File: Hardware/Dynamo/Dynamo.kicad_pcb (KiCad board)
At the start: 2 copper layers, 69.2 x 53.9 mm, 50 parts, among them U1 AP63205WU, U10 ESP32-S3-WROOM-1, U11 NCP1117-3.3_SOT223, U12 74AHC1G32, U13 TXS0102DCT, U14 TXS0102DCT, U15 74AHC1G32, U16 74AHC1G32, U17 74AHC1G32, U2 TLP2770, U3 TLP2770, U4 74LVC1G86, U5 74LVC1G86, U6 74LVC1G86, U7 74LVC1G86, U8 74LVC1G86, U9 74LVC1G86

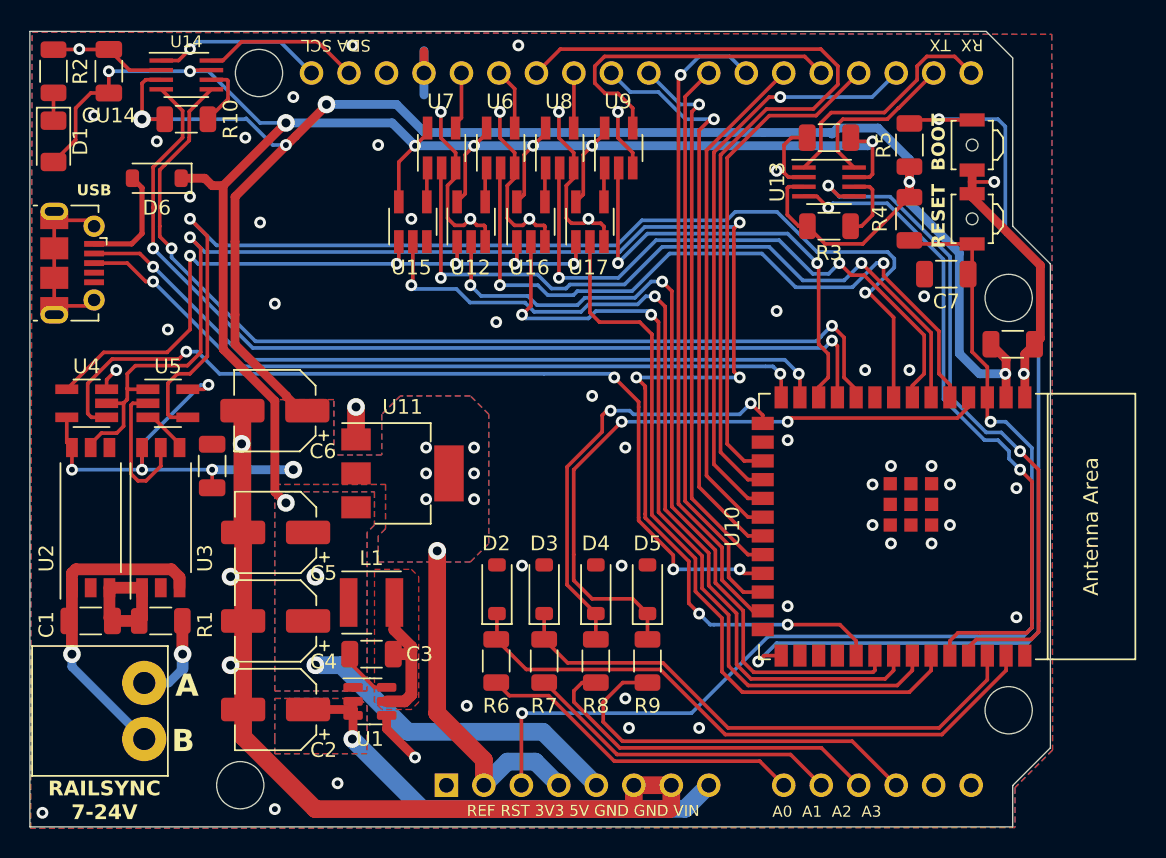
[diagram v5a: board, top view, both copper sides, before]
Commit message: Change Railsync input to use same 3.5mm connector as EX8874 outputs
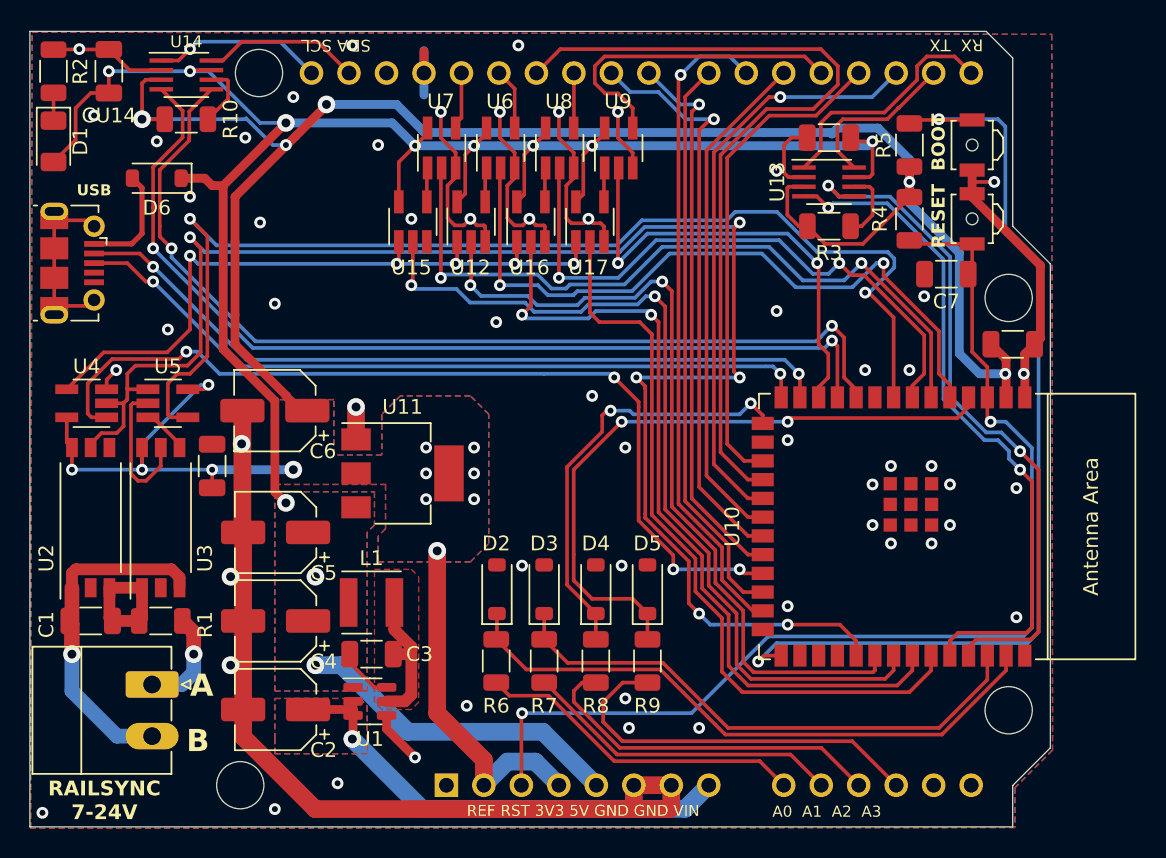
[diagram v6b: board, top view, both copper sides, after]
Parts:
- Railsync1: value WR-TBL 2P -> 2P 5mm; footprint Terminal_Wuerth_new:WR-TBL 2P -> Connector_Phoenix_MC:PhoenixContact_MC_1,5_2-G-3.5_1x02_P3.50mm_Horizontal
- moved Railsync1 3.96 mm to (129.9, 93.1)
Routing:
- net /RAILSYNC_B: track 21.6 -> 25.3 mm
- net /RAILSYNC_A: track 6.25 -> 6.97 mm

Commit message: Revised 5v regulator, layout refinement.
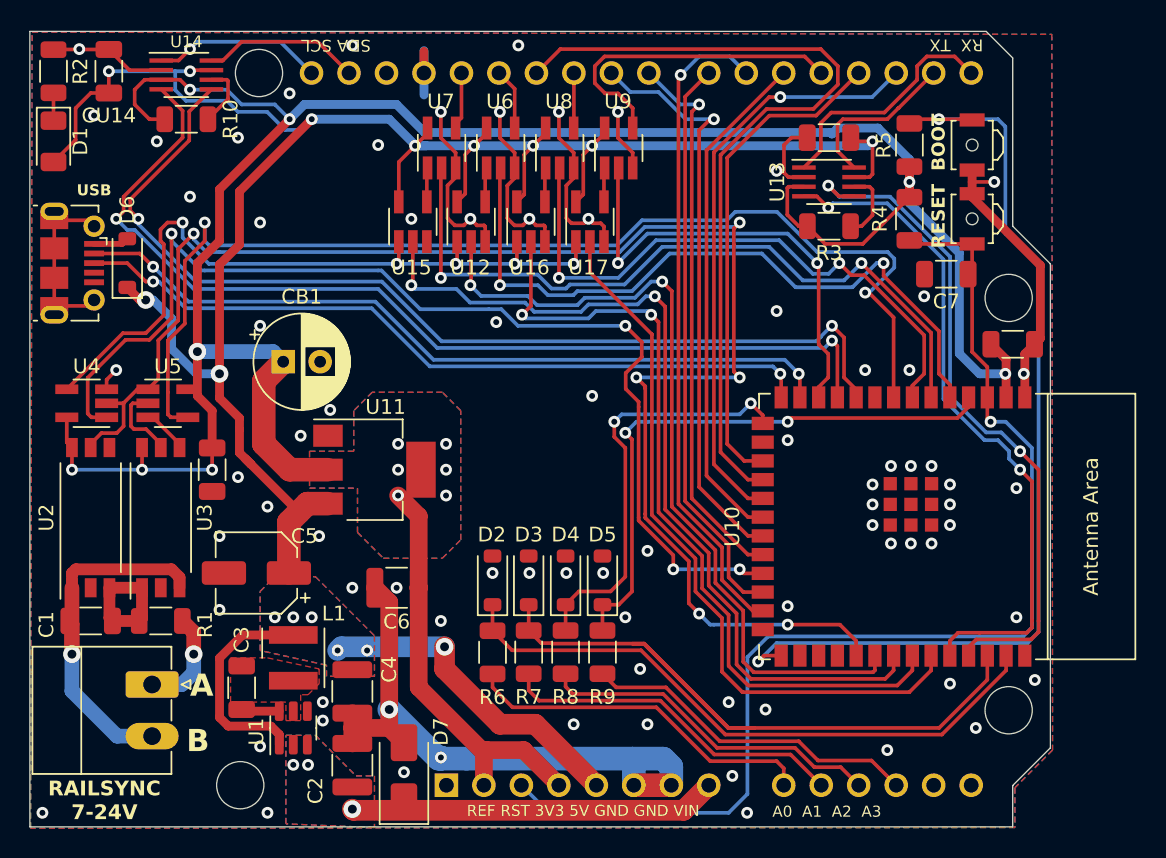
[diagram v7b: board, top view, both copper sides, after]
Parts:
- added CB1: 100uF, Capacitor_THT:CP_Radial_D6.3mm_P2.50mm, F.Cu at (138.8, 71.2)
- added D7: SMAJ18CA, Diode_SMD:D_SMA, F.Cu at (147.0, 99.0)
- C2, C4, C6: value 22uF -> 10uF; footprint Capacitor_SMD:CP_Elec_5x5.3 -> Capacitor_SMD:C_1210_3225Metric
- Railsync1: value 2P 5mm -> 2P 3.5mm
- moved C6 14.6 mm to (146.5, 86.5)
- moved C3 9.09 mm to (136.0, 93.3), turned to 90 degrees
- moved C4 7.06 mm to (143.5, 93.5), turned to -90 degrees
- moved L1 6.49 mm to (139.5, 91.2), turned to 90 degrees
- moved C2 6.43 mm to (143.5, 98.5), turned to 90 degrees
- moved D6 6.09 mm to (128.2, 64.5), turned to 90 degrees
- moved U1 5.49 mm to (139.5, 96.0), turned to 90 degrees
- moved R9 3.11 mm to (160.4, 90.9)
- moved D5 3.11 mm to (160.4, 86.0)
- moved C5 3.04 mm to (137.0, 85.5)
- moved R8 2.14 mm to (157.9, 90.9)
- moved D4 2.14 mm to (157.9, 86.0)
- moved U11 1.92 mm to (145.0, 78.5)
- moved R7 1.21 mm to (155.4, 90.9)
- moved D3 1.21 mm to (155.4, 86.0)
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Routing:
- net +5V: track 145.6 -> 179.7 mm, vias 11 -> 16
- net GND: track 160.4 -> 136.1 mm, vias 57 -> 80
- net /DIR_OVERRIDE: track 61.6 -> 75.4 mm
- net /A1p: track 37.3 -> 49.2 mm
- net Net-(U1-SW): track 9.92 -> 0.00 mm
- net +3.3V: track 175.1 -> 184.3 mm, vias 17 -> 14
- net VIN: track 32.4 -> 24.9 mm, vias 1 -> 3
- net Net-(D6-A): track 7.56 -> 2.39 mm
- net /A3p: track 44.3 -> 39.7 mm
- net Net-(U3-VO): track 9.74 -> 5.40 mm
- net /RESET: track 74.5 -> 78.6 mm, vias 2 -> 1
- net /A3: track 26.5 -> 23.0 mm
- net /DIR: track 47.5 -> 50.7 mm
- net /DIR_MONITOR: track 109.4 -> 106.2 mm
- net /SCL: track 65.2 -> 67.6 mm
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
